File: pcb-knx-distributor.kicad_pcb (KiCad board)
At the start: 2 copper layers, 113.5 x 25.6 mm, 17 parts, among them J1 Conn_01x02_Pin, J10 Conn_01x02_Pin, J11 Conn_01x02_Pin, J12 Conn_01x02_Pin, J13 Conn_01x02_Pin, J14 Conn_01x02_Pin, J2 Conn_01x02_Pin, J3 Conn_01x02_Pin, J4 Conn_01x02_Pin, J5 Conn_01x02_Pin, J6 Conn_01x02_Pin, J7 Conn_01x02_Pin, J8 Conn_01x02_Pin, J9 Conn_01x02_Pin

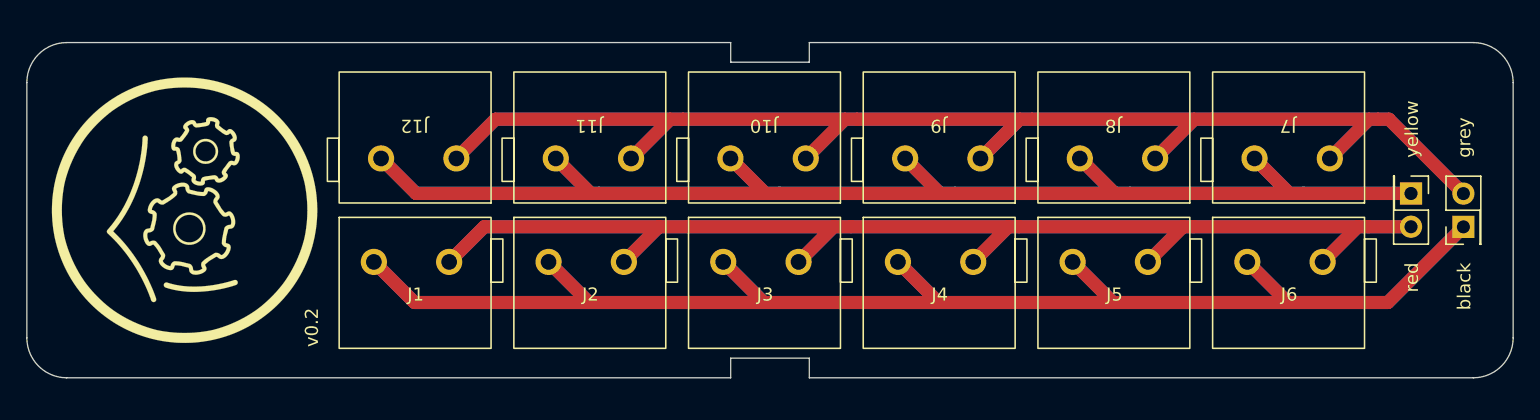
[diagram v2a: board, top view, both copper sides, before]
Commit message: Enlarged PCB
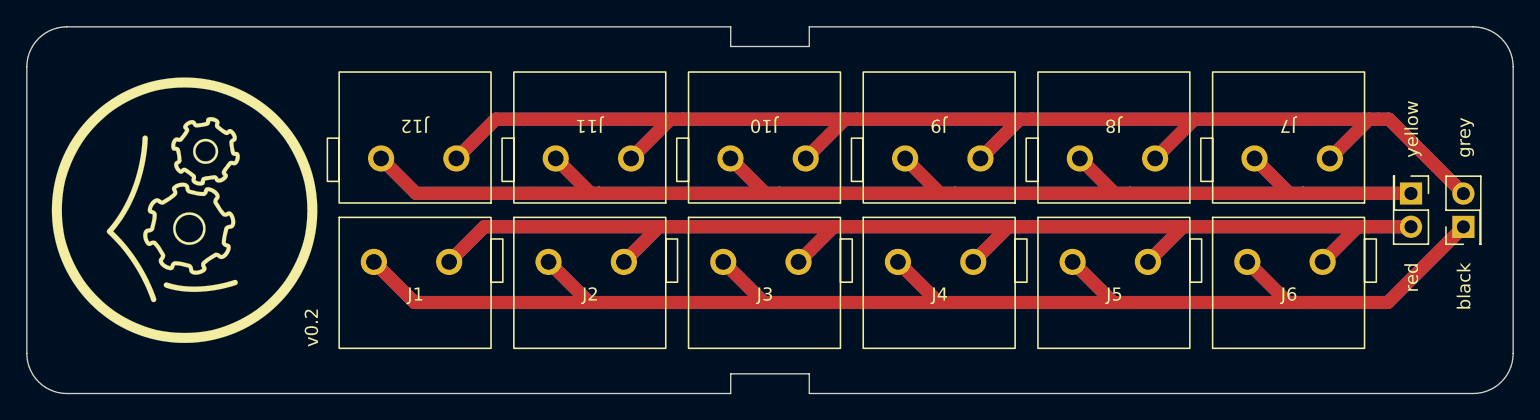
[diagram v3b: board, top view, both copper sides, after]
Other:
- board size 113.5 x 25.6 mm -> 113.5 x 28 mm
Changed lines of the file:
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@@
       (stroke (width 0.01) (type solid)) (fill solid) (layer "B.SilkS"))
   )
-  (gr_arc (start 135.75 73.75) (mid 134.856676 75.906676) (end 132.7 76.8)
+  (gr_arc (start 135.75 74.95) (mid 134.856676 77.106676) (end 132.7 78)
     (stroke (width 0.1) (type default)) (layer "Edge.Cuts"))
-  (gr_line (start 76 75.3) (end 82 75.3)
+  (gr_line (start 76 76.5) (end 82 76.5)
     (stroke (width 0.1) (type default)) (layer "Edge.Cuts"))
-  (gr_line (start 25.3 51.2) (end 76 51.2)
+  (gr_line (start 25.3 50) (end 76 50)
     (stroke (width 0.1) (type default)) (layer "Edge.Cuts"))
-  (gr_line (start 76 51.2) (end 76 52.7)
+  (gr_line (start 76 50) (end 76 51.5)
     (stroke (width 0.1) (type default)) (layer "Edge.Cuts"))
-  (gr_line (start 82 51.2) (end 132.7 51.2)
+  (gr_line (start 82 50) (end 132.7 50)
     (stroke (width 0.1) (type default)) (layer "Edge.Cuts"))
-  (gr_line (start 82 76.8) (end 132.7 76.8)
+  (gr_line (start 82 78) (end 132.7 78)
     (stroke (width 0.1) (type default)) (layer "Edge.Cuts"))
-  (gr_arc (start 25.3 76.8) (mid 23.143324 75.906676) (end 22.25 73.75)
+  (gr_arc (start 25.3 78) (mid 23.143324 77.106676) (end 22.25 74.95)
     (stroke (width 0.1) (type default)) (layer "Edge.Cuts"))
-  (gr_line (start 76 52.7) (end 82 52.7)
+  (gr_line (start 76 51.5) (end 82 51.5)
     (stroke (width 0.1) (type default)) (layer "Edge.Cuts"))
-  (gr_arc (start 22.25 54.25) (mid 23.143324 52.093324) (end 25.3 51.2)
+  (gr_arc (start 22.25 53.05) (mid 23.143324 50.893324) (end 25.3 50)
     (stroke (width 0.1) (type default)) (layer "Edge.Cuts"))
-  (gr_line (start 135.75 54.25) (end 135.75 73.75)
+  (gr_line (start 135.75 53.05) (end 135.75 74.95)
     (stroke (width 0.1) (type default)) (layer "Edge.Cuts"))
-  (gr_line (start 82 51.2) (end 82 52.7)
+  (gr_line (start 82 50) (end 82 51.5)
     (stroke (width 0.1) (type default)) (layer "Edge.Cuts"))
-  (gr_line (start 82 76.8) (end 82 75.3)
+  (gr_line (start 82 78) (end 82 76.5)
     (stroke (width 0.1) (type default)) (layer "Edge.Cuts"))
-  (gr_line (start 22.25 73.75) (end 22.25 54.25)
+  (gr_line (start 22.25 74.95) (end 22.25 53.05)
     (stroke (width 0.1) (type default)) (layer "Edge.Cuts"))
-  (gr_line (start 76 76.8) (end 76 75.3)
+  (gr_line (start 76 78) (end 76 76.5)
     (stroke (width 0.1) (type default)) (layer "Edge.Cuts"))
-  (gr_line (start 25.3 76.8) (end 76 76.8)
+  (gr_line (start 25.3 78) (end 76 78)
     (stroke (width 0.1) (type default)) (layer "Edge.Cuts"))
-  (gr_arc (start 132.7 51.2) (mid 134.856676 52.093324) (end 135.75 54.25)
+  (gr_arc (start 132.7 50) (mid 134.856676 50.893324) (end 135.75 53.05)
     (stroke (width 0.1) (type default)) (layer "Edge.Cuts"))
   (gr_text "red" (at 128.6 68 90) (layer "F.SilkS")
@@
   )
   (dimension (type aligned) (layer "F.SilkS")
-    (pts (xy 137.7 51.2) (xy 137.7 76.8))
+    (pts (xy 137.7 50) (xy 137.7 78))
     (height -6.9)
-    (gr_text "25.6000 mm" (at 143.45 64 90) (layer "F.SilkS")
+    (gr_text "28.0000 mm" (at 143.45 64 90) (layer "F.SilkS")
       (effects (font (size 1 1) (thickness 0.15)))
     )

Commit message: v0.3
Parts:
- added REF**: MountingHole_2mm, MountingHole:MountingHole_2mm, F.Cu at (25.3, 53.0)
- added REF**: MountingHole_2mm, MountingHole:MountingHole_2mm, F.Cu at (132.7, 53.0)
- added REF**: MountingHole_2mm, MountingHole:MountingHole_2mm, F.Cu at (132.7, 75.0)
- added REF**: MountingHole_2mm, MountingHole:MountingHole_2mm, F.Cu at (25.3, 75.0)
- moved REF** 80.8 mm to (49.1, 64.0)
- moved J12 12.2 mm to (57.8, 51.2), turned to -90 degrees
- moved J1 11.6 mm to (57.8, 64.5), turned to -90 degrees
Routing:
- net /black: track 217.6 -> 198.3 mm
- net /yellow: track 197.3 -> 180.0 mm
- net /red: track 187.1 -> 200.4 mm
- net /grey: track 203.4 -> 205.0 mm
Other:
- board text added: "haus-automatisierung.com"
- board text added: "v0.3"
- board text removed: "v0.2"

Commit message: 0.4
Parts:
- removed G***: LOGO, haus-automatisierung:Logo_20mm
- removed G***: LOGO, haus-automatisierung:QRCode-hausauto_20mm
- removed the REF** at (25.3, 53.0)
- removed the REF** at (132.7, 53.0)
- removed the REF** at (132.7, 75.0)
- removed the REF** at (25.3, 75.0)
- added J14: Conn_01x02_Pin, haus-automatisierung:Wago-243-211, F.Cu at (46.4, 64.6)
- added J8: Conn_01x02_Pin, haus-automatisierung:Wago-243-212, F.Cu at (124.7, 63.5)
- added REF**: MountingHole_2.5mm, MountingHole:MountingHole_2.5mm, F.Cu at (131.9, 53.0)
- added REF**: MountingHole_2.5mm, MountingHole:MountingHole_2.5mm, F.Cu at (31.1, 53.0)
- added REF**: MountingHole_2.5mm, MountingHole:MountingHole_2.5mm, F.Cu at (131.9, 75.0)
- added REF**: MountingHole_2.5mm, MountingHole:MountingHole_2.5mm, F.Cu at (31.1, 75.0)
- added REF**: KiCad-Logo2_6mm_SilkScreen, Symbol:KiCad-Logo2_6mm_SilkScreen, B.Cu at (34.4, 64.0)
- J11: renamed from J4; footprint haus-automatisierung:Wago-243-211 -> haus-automatisierung:Wago-243-212
- J13: renamed from J2; footprint haus-automatisierung:Wago-243-211 -> haus-automatisierung:Wago-243-212
- J3: renamed from J11; footprint haus-automatisierung:Wago-243-212 -> haus-automatisierung:Wago-243-211
- J5: renamed from J9; footprint haus-automatisierung:Wago-243-212 -> haus-automatisierung:Wago-243-211
- J7: footprint haus-automatisierung:Wago-243-212 -> haus-automatisierung:Wago-243-211
- J9: renamed from J6; footprint haus-automatisierung:Wago-243-211 -> haus-automatisierung:Wago-243-212
- moved REF** 72.4 mm to (121.5, 64.0)
- moved J1 13.1 mm to (44.6, 64.5)
- moved J2 13.1 mm to (44.6, 51.2)
- moved J7 13.1 mm to (111.3, 63.5)
- moved J6 13.1 mm to (98.0, 63.5)
- moved J5 13.1 mm to (84.7, 63.5)
- moved J4 13.1 mm to (71.3, 63.5)
- moved J3 13.1 mm to (58.0, 63.5)
- moved J13 0.28 mm to (59.7, 64.6)
- moved J12 0.27 mm to (73.0, 64.6)
- moved J11 0.26 mm to (86.4, 64.6)
- moved J10 0.25 mm to (99.7, 64.6)
- moved J9 0.24 mm to (113.0, 64.6)
- moved J16 0.15 mm to (127.8, 62.7)
- moved J15 0.15 mm to (131.8, 65.3)
- renumbered J5 to J10, J3 to J12, J13 to J15, J14 to J16, J12 to J2, J10 to J4, J8 to J6
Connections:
- J11 pad 1: /black -> /grey
- J11 pad 2: /red -> /yellow
- J13 pad 1: /black -> /grey
- J13 pad 2: /red -> /yellow
- J3 pad 1: /grey -> /black
- J3 pad 2: /yellow -> /red
- J5 pad 1: /grey -> /black
- J5 pad 2: /yellow -> /red
- J7 pad 1: /grey -> /black
- J7 pad 2: /yellow -> /red
- J9 pad 1: /black -> /grey
- J9 pad 2: /red -> /yellow
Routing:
- net /red: track 200.4 -> 145.6 mm
- net /grey: track 205.0 -> 161.5 mm
- net /black: track 198.3 -> 156.8 mm
- net /yellow: track 180.0 -> 153.1 mm
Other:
- board size 113.5 x 28 mm -> 107 x 28 mm
- board text added: "B"
- board text added: "G"
- board text added: "R"
- board text added: "Y"
- board text added: "v0.4"
- board text removed: "v0.3"

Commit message: v0.5
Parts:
- removed the REF** at (131.9, 53.0)
- removed the REF** at (31.1, 53.0)
- removed the REF** at (131.9, 75.0)
- removed the REF** at (31.1, 75.0)
- removed the REF** at (121.5, 64.0)
- removed the REF** at (34.4, 64.0)
- added REF**: MountingHole_2.7mm, MountingHole:MountingHole_2.7mm, F.Cu at (31.1, 75.0)
- added REF**: MountingHole_2.7mm, MountingHole:MountingHole_2.7mm, F.Cu at (131.9, 53.0)
- added REF**: MountingHole_2.7mm, MountingHole:MountingHole_2.7mm, F.Cu at (31.1, 53.0)
- added REF**: MountingHole_2.7mm, MountingHole:MountingHole_2.7mm, F.Cu at (131.9, 75.0)
- J10, J12, J14: footprint haus-automatisierung:Wago-243-211 -> haus-automatisierung:Wago-243-212
- J11, J13, J9: footprint haus-automatisierung:Wago-243-212 -> haus-automatisierung:Wago-243-211
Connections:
- J10 pad 1: /black -> /grey
- J10 pad 2: /red -> /yellow
- J11 pad 1: /grey -> /black
- J11 pad 2: /yellow -> /red
- J12 pad 1: /black -> /grey
- J12 pad 2: /red -> /yellow
- J13 pad 1: /grey -> /black
- J13 pad 2: /yellow -> /red
- J14 pad 1: /black -> /grey
- J14 pad 2: /red -> /yellow
- J9 pad 1: /grey -> /black
- J9 pad 2: /yellow -> /red
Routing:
- net /grey: track 161.5 -> 168.9 mm
- net /yellow: track 153.1 -> 147.1 mm
- net /black: track 156.8 -> 159.3 mm
- net /red: track 145.6 -> 144.9 mm
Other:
- board text added: "v0.5"
- board text removed: "black"
- board text removed: "grey"
- board text removed: "red"
- board text removed: "yellow"

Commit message: KiCad 8
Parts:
- added G***: LOGO, haus-automatisierung:knx_deutschland, B.Cu at (34.4, 64.0)
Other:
- board text added: "v0.6"
- board text removed: "v0.5"

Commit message: v0.6
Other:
- board text removed: "v0.4"
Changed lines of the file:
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@@
 	(title_block
 		(title "KNX Distributor")
-		(date "2024-04-30")
+		(date "2024-05-30")
 		(rev "0.6")
 		(company "haus-automatisierung.com")
@@
 		)
 	)
-	(gr_text "v0.4"
-		(at 44.45 74.45 90)
-		(layer "F.SilkS")
-		(effects
-			(font
-				(size 1 1)
-				(thickness 0.15)
-			)
-			(justify left bottom)
-		)
-	)
